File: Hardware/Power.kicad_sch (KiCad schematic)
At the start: 24 parts, among them U1 MPM3834CGPA-Z, U2 MPM3834CGPA-Z, U4 TPS3106K33DBVR

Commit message: 11/17 progress update
finished the board, now just need to add the peripheral
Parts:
- added C28, C7: 4.7uF, Capacitor_SMD:C_0201_0603Metric, symbol Device:C
- added J2, J3: USB_C_Receptacle_USB2.0, Connector_USB:USB_C_Receptacle_Palconn_UTC16-G, symbol Connector:USB_C_Receptacle_USB2.0
- added L2: 2.2uH, Capacitor_SMD:C_1812_4532Metric, symbol Device:L
- added MT1, MT2, MT3, MT4: Mounting, MountingHole:MountingHole_3.2mm_M3_ISO7380_Pad, symbol Connector:Conn_01x01_Pin
- added R35, R36, R37, R38, R39: 10k, Capacitor_SMD:C_0402_1005Metric, symbol Device:R
- added SS2FH10HM3/H1, SS2FH10HM3/H2: B5819W, Diode_SMD:D_SMF, symbol Device:D_Schottky
- added TP6, TP7: TP, TestPoint:TestPoint_Pad_1.0x1.0mm, symbol Connector:Conn_01x01_Pin
- added U10: SC189ZULTRT-3v3, Package_TO_SOT_SMD:SOT-23-5, symbol Personal:SC189ZULTRT-3.3
- added U9: ZL6201A33S3, Package_TO_SOT_SMD:SOT-23, symbol Regulator_Linear:XC6206PxxxMR
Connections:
- net +3V3: now also L2.2, U10.4 (VOUT)
- net GND: now also C28.2, C7.2, J2.A1 (GND), J2.A12 (GND), J2.B1 (GND), J2.B12 (GND), J2.S1 (SHIELD), J3.A1 (GND), J3.A12 (GND), J3.B1 (GND), J3.B12 (GND), J3.S1 (SHIELD), MT1.1 (Pin_1), MT2.1 (Pin_1), MT3.1 (Pin_1), MT4.1 (Pin_1), R35.1, R36.1, R37.1, R38.1, U10.2 (GND), U9.1 (GND)
- new net: J2.A4 (VBUS), J2.A9 (VBUS), J2.B4 (VBUS), J2.B9 (VBUS), SS2FH10HM3/H2.2 (A)
- new net: J2.A5 (CC1), R35.2
- new net: J2.B5 (CC2), R36.2
- new net: J3.A5 (CC1), R37.2
- new net: J3.B5 (CC2), R38.2
- new net: L2.1, U10.5 (LX)
- new net: R39.2, TP6.1 (Pin_1), U10.3 (EN)
- new net +3.3VA: C28.1, C7.1, U9.2 (VO)
- new net +5V: J3.A4 (VBUS), J3.A9 (VBUS), J3.B4 (VBUS), J3.B9 (VBUS), SS2FH10HM3/H1.2 (A), SS2FH10HM3/H2.1 (K), U9.3 (VI)
- new net +5VP: R39.1, SS2FH10HM3/H1.1 (K), TP7.1 (Pin_1), U10.1 (VIN)
- new net USB+: J2.A6 (D+), J2.B6 (D+)
- new net USB-: J2.A7 (D-), J2.B7 (D-)
- new net oUSB+: J3.A6 (D+), J3.B6 (D+)
- new net oUSB-: J3.A7 (D-), J3.B7 (D-)
- no-connect marks 2 -> 6

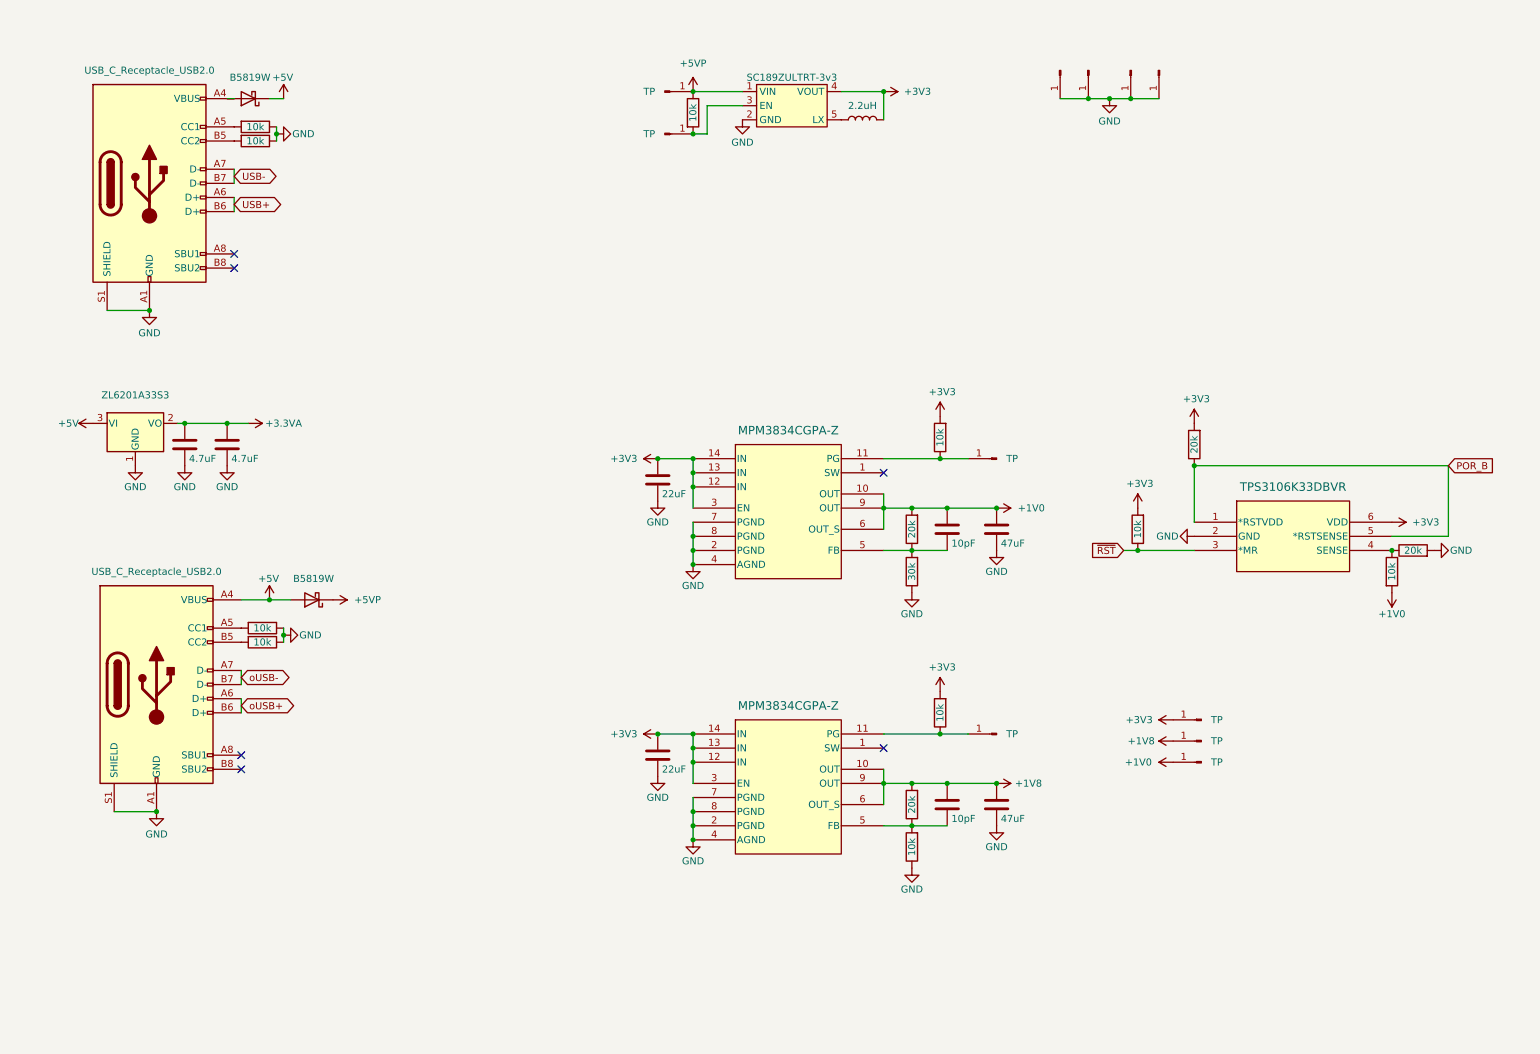
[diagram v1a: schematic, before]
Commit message: 11/19 update
add new header for jtag and fixed a couple of small things
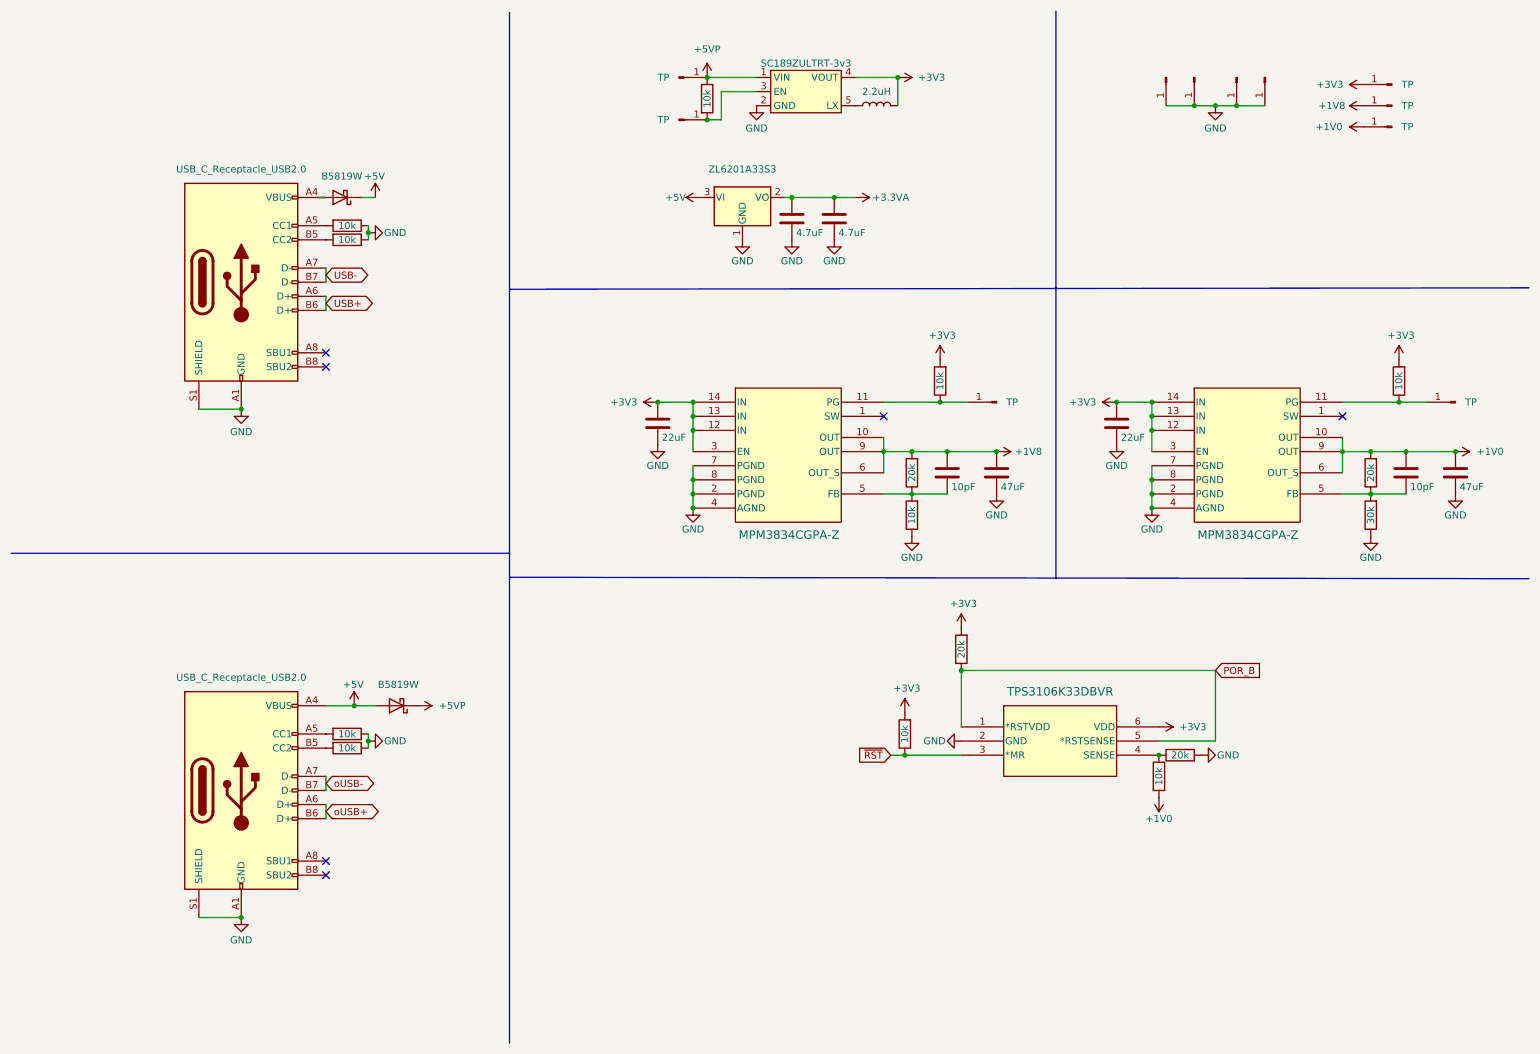
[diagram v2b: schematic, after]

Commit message: 11/21 update
finished annotating the schematic and add pictures and output the pdf
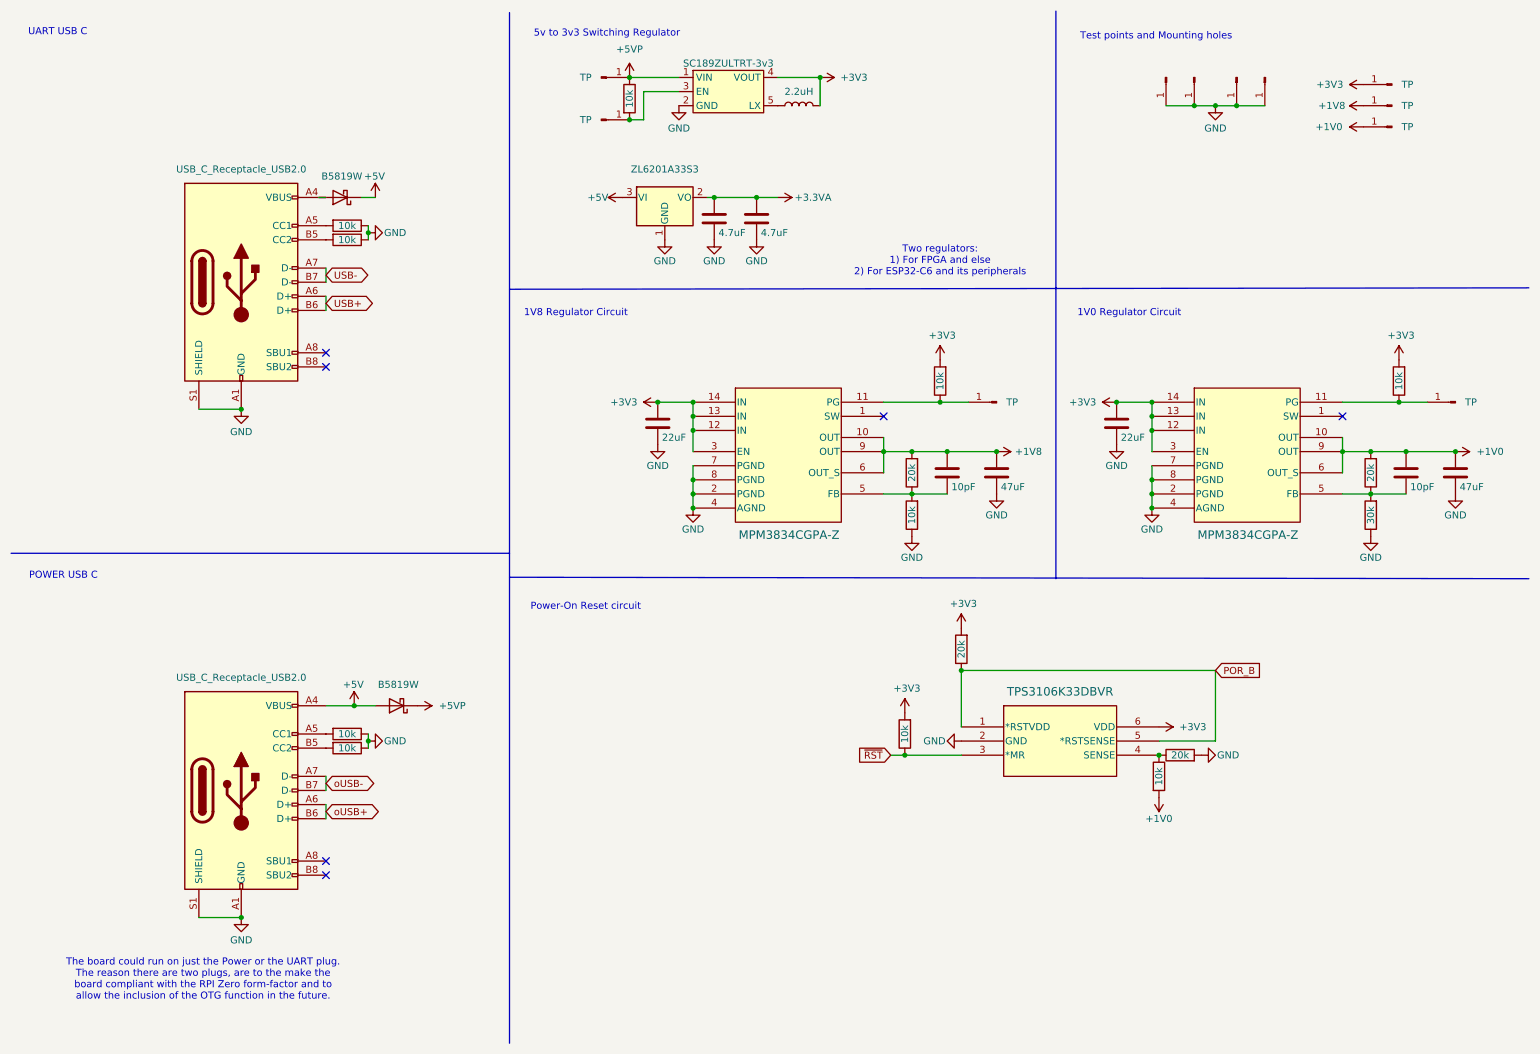
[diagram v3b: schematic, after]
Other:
- note added: "1V0 Regulator Circuit"
- note added: "1V8 Regulator Circuit"
- note added: "5v to 3v3 Switching Regulator"
- note added: "POWER USB C"
- note added: "Power-On Reset circuit"
- note added: "Test points and Mounting holes"
- note added: "The board could run on just the Power or the UART plug. The reason there are two plugs, are to the make the board compliant with the RPI Zero form-factor and to allow the inclusion of the OTG function in the future."
- note added: "Two regulators: 1) For FPGA and else 2) For ESP32-C6 and its peripherals"
- note added: "UART USB C"
